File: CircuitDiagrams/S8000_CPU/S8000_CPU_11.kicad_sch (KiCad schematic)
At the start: 0 parts

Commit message: page 11 done
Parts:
- added C42: 22uF/25V, symbol Device:C_Polarized_Small_US
- added CR1: 1N4001, Diode_THT:D_DO-41_SOD81_P10.16mm_Horizontal, symbol Diode:1N4001
- added DS1, DS2, DS3, DS4: LED, symbol Device:LED
- added R15: 10k, Resistor_THT:R_Axial_DIN0207_L6.3mm_D2.5mm_P7.62mm_Horizontal, symbol Device:R_US
- added R16, R17, R18: 1k, Resistor_THT:R_Axial_DIN0207_L6.3mm_D2.5mm_P7.62mm_Horizontal, symbol Device:R_US
- added U10: AM93S16, symbol S8000:AM93S16
- added U109: 74LS240, symbol 74xx:74LS240
- added U78: 7411, symbol 74xx:74LS11
- added U79, U80: Z80_CLK_DRV, symbol S8000:Z80_CLK_DRV
- added U81: 7414, symbol 74xx:74LS14
- added U83: 74113, symbol 74xx:74LS113
- added U84: 2.4576 MHz, Oscillator:Oscillator_DIP-14, symbol Oscillator:ACO-xxxMHz
- added U85: 44.440 MHz, Oscillator:Oscillator_DIP-14, symbol Oscillator:ACO-xxxMHz
- added U95: 7404, symbol 74xx:74LS04
- added U96: 7408, symbol 74xx:74LS08
- added U97: 7474, symbol 74xx:74LS74
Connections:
- new net: U109.17 (I3b), U97.6 (~{Q})
- new net: U109.2 (I0a), U79.3 (IN), U95.3, U96.11
- new net: DS1.1 (K), U109.3 (O3b)
- new net: U109.4 (I1a), U78.2, U95.13, U96.3
- new net: DS4.1 (K), U109.5 (O2b)
- new net: R16.2, U78.11, U97.1 (~{R}), U97.13 (~{R})
- new net: U78.8, U83.4 (~{S})
- new net: U78.9, U81.8
- new net: U83.13 (C), U84.8 (OUT)
- new net: U78.12, U97.3 (C)
- new net: U10.14 (O0), U96.1, U96.2
- new net: U78.6, U97.10 (~{S})
- new net: U81.6, U81.9
- new net: U10.12 (O2), U96.10, U96.12, U96.13
- new net: U80.3 (IN), U96.8
- new net: U96.9, U97.5 (Q)
- new net: R17.2, U10.1 (MR), U10.10 (CET), U10.3 (P0), U10.4 (P1), U10.5 (P2), U10.6 (P3), U10.7 (CEP), U10.9 (PE)
- new net: U10.13 (O1), U96.4, U96.5
- new net: U10.2 (CP), U85.8 (OUT)
- new net: U95.1, U95.12
- new net: U97.4 (~{S}), U97.8 (~{Q})
- new net: U95.11, U96.6
- new net +5V: CR1.1 (K), DS1.2 (A), DS2.2 (A), DS3.2 (A), DS4.2 (A), R15.1, R16.1, R17.1, R18.1, U10.16 (VCC), U109.20 (VCC), U79.1 (V+), U80.1 (V+), U84.14 (Vcc), U85.14 (Vcc)
- new net BAUD CLK: U83.9 (Q)
- new net BUSACKH: U109.19 (OEb), U109.6 (I2a)
- new net BUS_BCLK: U109.18 (O0a)
- new net BUS_MCLK: U109.16 (O1a)
- new net BUS_~{AS}: U109.9 (O0b)
- new net BUS_~{DS}: U109.7 (O1b)
- new net BUS_~{POWERFAIL}: R18.2, U81.3, U83.2 (K)
- new net BUS_~{WAIT}: U97.2 (D)
- new net CLOCK A: U80.6 (OUT)
- new net CLOCK B: U79.6 (OUT), U97.11 (C)
- new net GND: C42.2, U10.8 (GND), U109.1 (OEa), U109.10 (GND), U79.5 (GND), U80.5 (GND), U83.10 (~{S}), U83.11 (J), U83.12 (K), U83.3 (J), U84.7 (GND), U85.7 (GND)
- new net INT 2 PHI: U95.10, U95.9
- new net INT PHI: U78.1, U83.1 (C), U95.4, U95.5
- new net IN/~{S}: U109.8 (I3a)
- new net LATCHECCERROR: U109.15 (I2b)
- new net P2_FP_BUSACK_INDICATOR: DS3.1 (K), U109.14 (O2a)
- new net P2_FP_NORMAL_INDICATOR: DS2.1 (K), U109.12 (O3a)
- new net P2_SW_~{RESET}: C42.1, CR1.2 (A), R15.2, U81.5
- new net PHI DELAY: U78.13
- new net POWERFAIL: U81.4
- new net SYS AS: U109.11 (I0b)
- new net SYS DS: U109.13 (I1b)
- new net ~{EPUXFER}: U78.3
- new net ~{IDS}: U97.12 (D)
- new net ~{INT 4 PHI}: U95.2
- new net ~{INT PHI}: U95.6
- new net ~{I/O_REF}: U78.4
- new net ~{MRESET}: U78.5, U83.6 (~{Q})
- new net ~{SOFTRESET}: U78.10
- no-connect marks 0 -> 5
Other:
- note added: "(Sh. 10,12,14)"
- note added: "(Sh. 12)"
- note added: "(Sh. 13)"
- note added: "(Sh. 13,14)"
- note added: "(Sh. 14)"
- note added: "(Sh. 2)"
- note added: "(Sh. 2,8)"
- note added: "(Sh. 3)"
- note added: "(Sh. 4)"
- note added: "(Sh. 4,5,6,7,14)"
- note added: "(Sh. 4,7)"
- note added: "(Sh. 8)"
- note added: "1.1"
- note added: "Clock Generation Circuit (U98) Baud Clock Generator (U83) System Reset Logic (U89) T3 Wait State Generator Logic (U97)"
- note added: "Oliver Lehmann <lehmann@ans-netz.de>"
- note added: "P1 - 12B"
- note added: "P1 - 12C"
- note added: "P1 - 27C"
- note added: "P1-27A"
- note added: "P2 - 22C"
- note added: "P2 - 24C"
- note added: "P2-27A"
- note added: "Zilog S8000 CPU"

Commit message: page 12 done
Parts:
- U109: value 74LS240 -> 74240
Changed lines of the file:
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@@
 			)
 		)
-		(property "Value" "74LS240"
+		(property "Value" "74240"
 			(at 423.7833 328.93 0)
 			(show_name no)

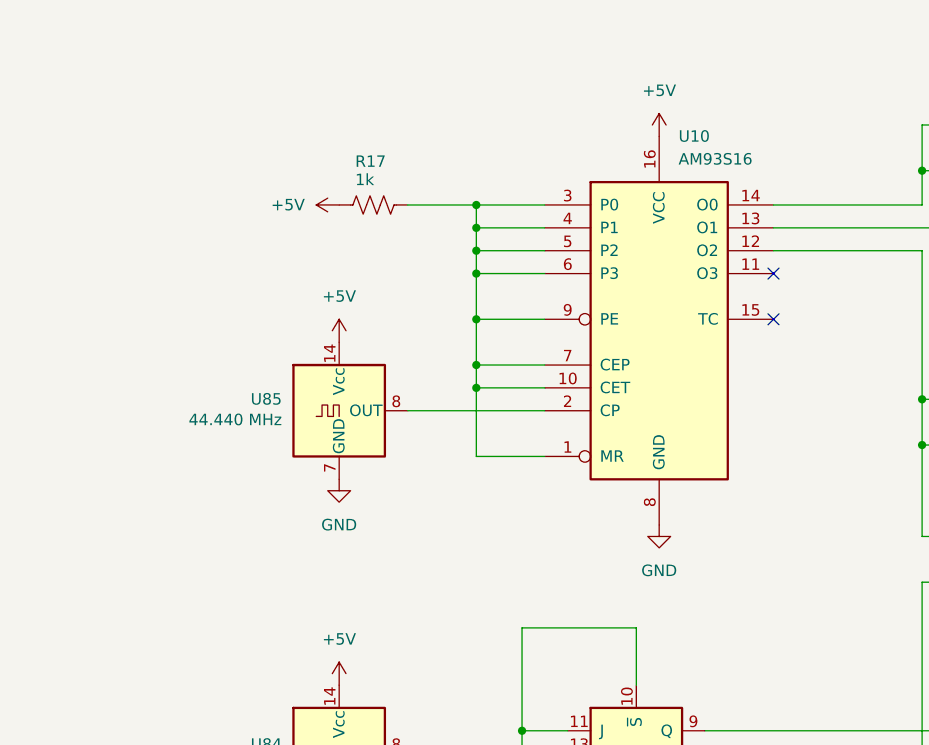
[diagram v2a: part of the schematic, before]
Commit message: U98 is a 74S161/93S16
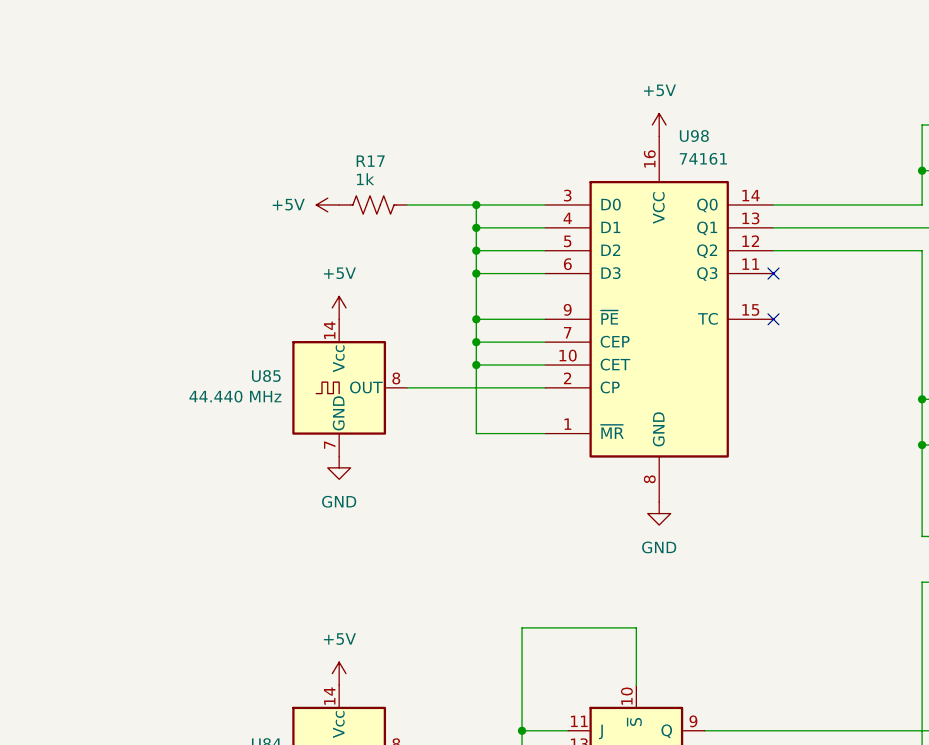
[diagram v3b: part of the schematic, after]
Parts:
- removed U10: AM93S16, symbol S8000:AM93S16
- added U98: 74161, symbol 74xx:74LS161
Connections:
- net +5V: now also U98.16 (VCC)
- net GND: now also U98.8 (GND)
- net at U96.1, U96.2: now also U98.14 (Q0)
- net at U96.10, U96.12, U96.13: now also U98.12 (Q2)
- net at R17.2: now also U98.1 (~{MR}), U98.10 (CET), U98.3 (D0), U98.4 (D1), U98.5 (D2), U98.6 (D3), U98.7 (CEP), U98.9 (~{PE})
- net at U96.4, U96.5: now also U98.13 (Q1)
- net at U85.8 (OUT): now also U98.2 (CP)
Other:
- moved on the sheet: U85

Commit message: add notes
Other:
- note added: "on some boards 93S16"
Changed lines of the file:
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@@
+		)
+	)
+	(text "on some boards\n93S16"
+		(exclude_from_sim no)
+		(at 154.432 66.04 0)
+		(effects
+			(font
+				(size 1.27 1.27)
+			)
+			(justify left)
 		)
 	)
